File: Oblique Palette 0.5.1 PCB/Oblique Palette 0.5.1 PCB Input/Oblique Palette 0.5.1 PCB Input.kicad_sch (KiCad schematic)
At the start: 24 parts

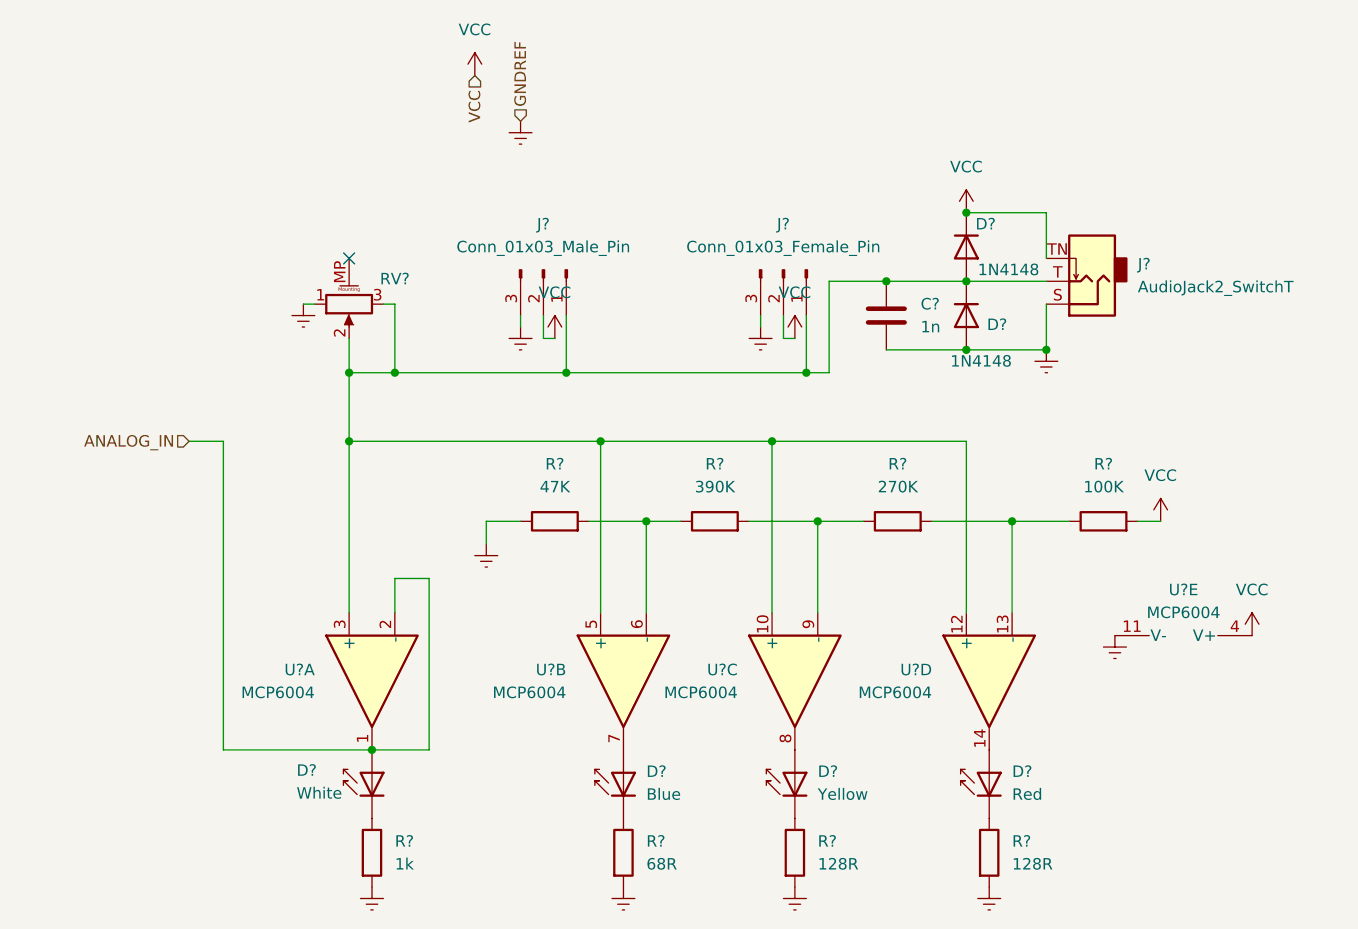
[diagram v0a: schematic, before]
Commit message: PCB corrections for 0.5.3
• Main output LED is now between op amp and feedback loop, so it will brighten at the first whiff of voltage.
• Errant wire between VBus and input potentiometer will allow us to have signals other than 5V
• Servos are now powered by V_SERVO as well as VBus.

TO DO: Differentiate A0 and A1 DACs
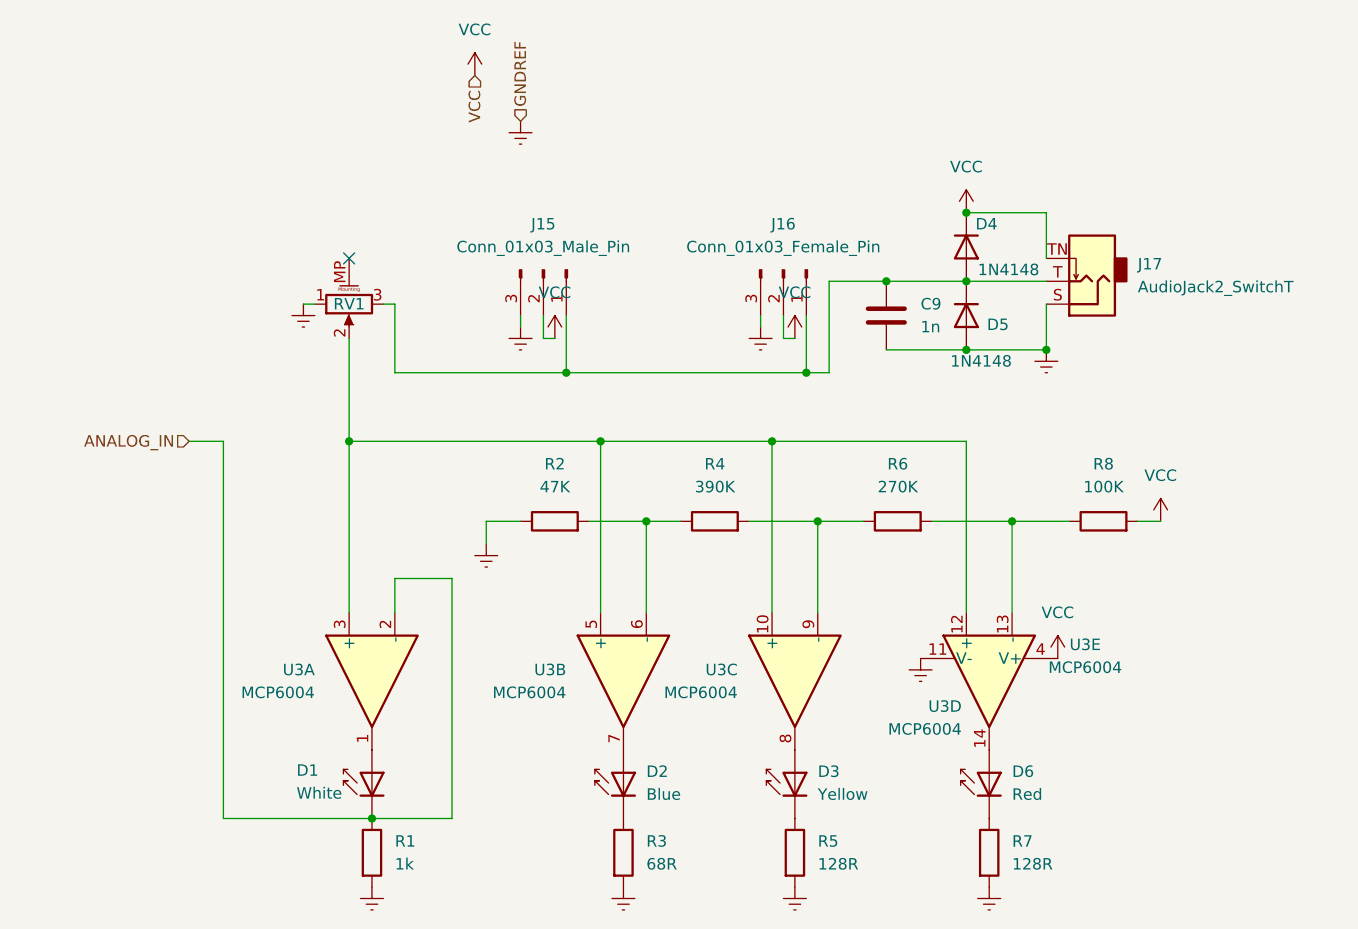
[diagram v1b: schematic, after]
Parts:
- gave numbers to parts that had none: 20
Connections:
- net ANALOG_IN: now also D1.1 (K), R1.1; no longer D1.2 (A), U3.1
- net at C9.1, D4.2 (A), D5.1 (K)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: no longer RV1.2, U3.10 (+), U3.12 (+), U3.3 (+), U3.5 (+)
- new net: D1.2 (A), U3.1
- new net: RV1.2, U3.10 (+), U3.12 (+), U3.3 (+), U3.5 (+)
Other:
- moved on the sheet: U3E

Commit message: Corrected op amp circuits on INPUT
Reduced from 4 LED indicators to 3, plus output.

WHITE now glows increasing brightness from >0V up to 5V
YELLOW turns on at 2.7V (a logical HIGH)
RED turns on at 3.6V (the danger level for 3V circuits)

The remaining op amp is now purely an output, now with a 1k resistor to reduce whoopsies while in use.
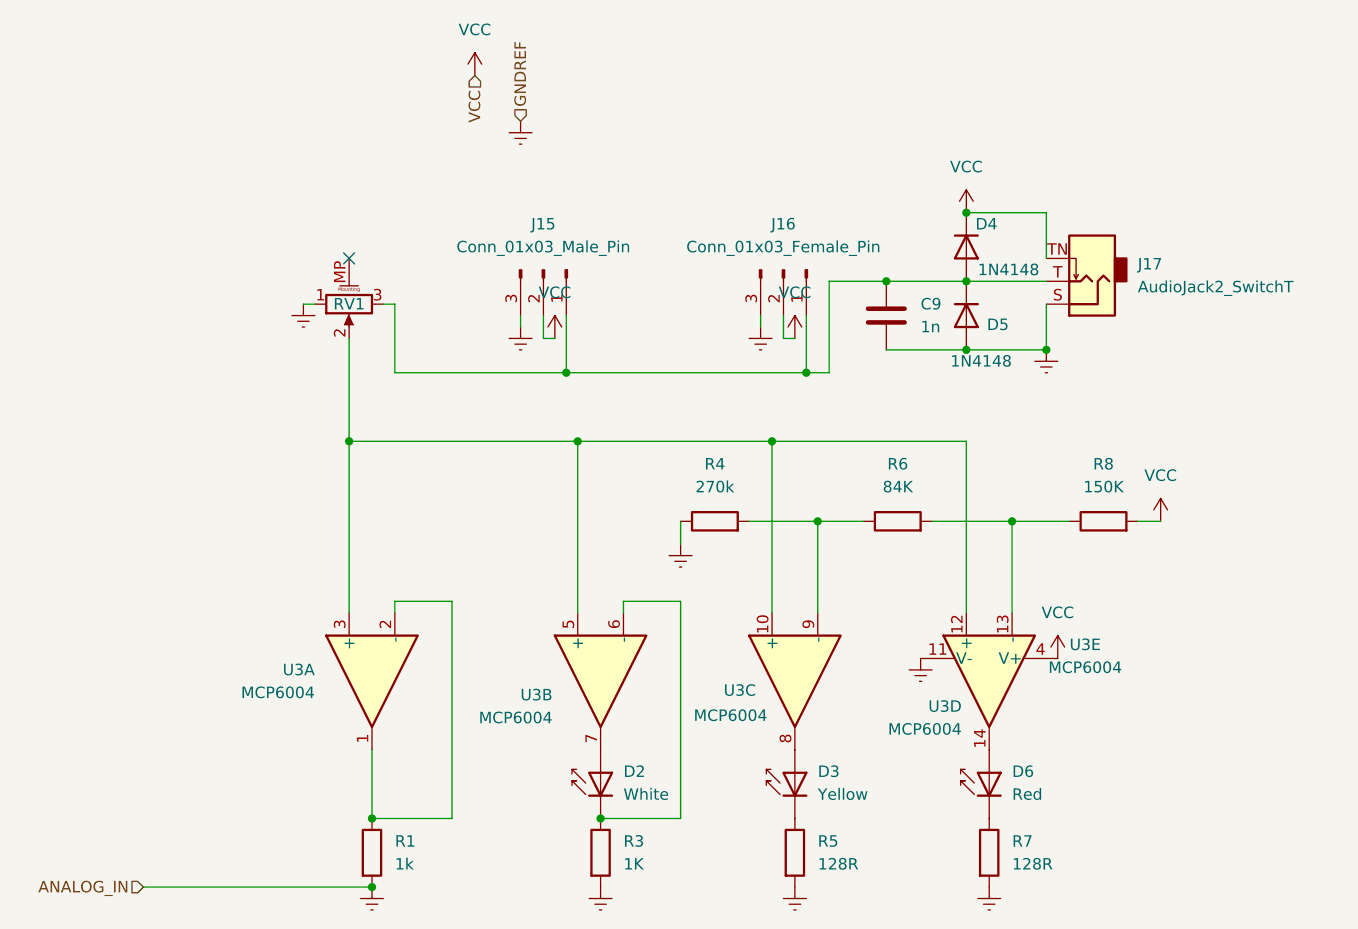
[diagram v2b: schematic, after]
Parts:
- removed D1: White, LED_THT:LED_SideEmitter_Rectangular_W4.5mm_H1.6mm, symbol LED:IRL81A
- removed R2: 47K, Resistor_SMD:R_0805_2012Metric, symbol Device:R
- D2: value Blue -> White
- R3: value 68R -> 1K
- R4: value 390K -> 270k
- R6: value 270K -> 84K
- R8: value 100K -> 150K
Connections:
- net ANALOG_IN is gone; now on an unnamed net: R1.1, U3.2 (-)
- net GNDREF: now also R4.1
- net at U3.6 (-): now also D2.1 (K), R3.1; no longer R4.1
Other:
- moved on the sheet: D2, R3, U3B

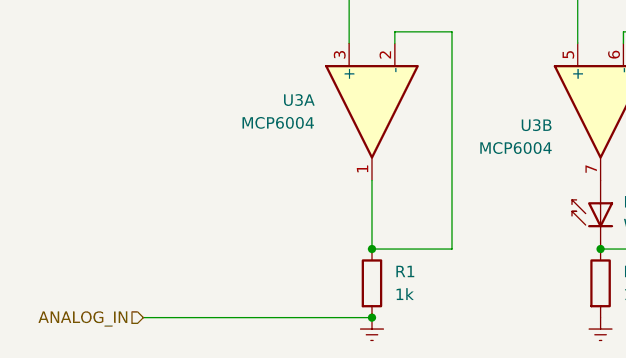
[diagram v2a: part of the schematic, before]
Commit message: Deleted redundant resistor
Realized that the input between the op amp and the µC pin didn't need a current-limiting resistor because we know exactly what's going to be there.
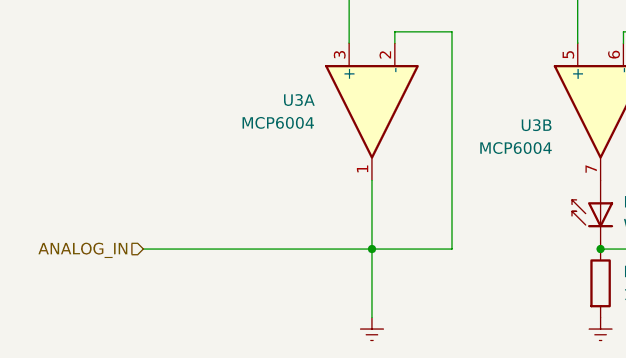
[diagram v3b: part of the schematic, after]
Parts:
- removed R1: 1k, Resistor_SMD:R_0805_2012Metric, symbol Device:R
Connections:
- net GNDREF: now also U3.1, U3.2 (-)
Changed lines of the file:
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@@
 	)
 	(junction
-		(at 105.41 128.27)
-		(diameter 0)
-		(color 0 0 0 0)
-	)
-	(junction
 		(at 149.86 78.74)
 		(diameter 0)
@@
 	(wire
 		(pts
-			(xy 80.01 128.27) (xy 105.41 128.27)
+			(xy 80.01 120.65) (xy 105.41 120.65)
 		)
 		(stroke
@@
 	(wire
 		(pts
+			(xy 105.41 120.65) (xy 105.41 128.27)
+		)
+		(stroke
+			(width 0)
+			(type default)
+		)
+	)
+	(wire
+		(pts
 			(xy 176.53 87.63) (xy 176.53 97.79)
 		)
@@
 	(hierarchical_label "ANALOG_IN"
 		(shape input)
-		(at 80.01 128.27 180)
+		(at 80.01 120.65 180)
 		(effects
 			(font
@@
 					(unit 1)
 				)
-			)
-		)
-	)
-	(symbol
-		(lib_id "Device:R")
-		(at 105.41 124.46 0)
-		(unit 1)
-		(exclude_from_sim no)
-		(in_bom yes)
-		(on_board yes)
-		(dnp no)
-		(fields_autoplaced yes)
-		(property "Reference" "R1"
-			(at 107.95 123.1899 0)
-			(effects
-				(font
-					(size 1.27 1.27)
-				)
-				(justify left)
-			)
-		)
-		(property "Value" "1k"
-			(at 107.95 125.7299 0)
-			(effects
-				(font
-					(size 1.27 1.27)
-				)
-				(justify left)
-			)
-		)
-		(property "Footprint" "Resistor_SMD:R_0805_2012Metric"
-			(at 103.632 124.46 90)
-			(effects
-				(font
-					(size 1.27 1.27)
-				)
-				(hide yes)
-			)
-		)
-		(property "Datasheet" "~"
-			(at 105.41 124.46 0)
-			(effects
-				(font
-					(size 1.27 1.27)
-				)
-				(hide yes)
-			)
-		)
-		(property "Description" "Resistor"
-			(at 105.41 124.46 0)
-			(effects
-				(font
-					(size 1.27 1.27)
-				)
-				(hide yes)
-			)
-		)
-		(pin "2"
-		)
-		(pin "1"
-		)
-		(instances
-			(project "Oblique Palette 0.4 Input Stage"
-				(path "/150b6f87-53bb-44d6-889a-48fbcb7c0f5a"
-					(reference "R?")
-					(unit 1)
-				)
-			)
-			(project "Oblique Palette 0.5.1 PCB Main"
-				(path "/28718c51-05fa-44bf-9e59-30883fb9ecef/10bc258e-81e1-44f3-990d-192650ef1d17"
-					(reference "R25")
-					(unit 1)
-				)
-				(path "/28718c51-05fa-44bf-9e59-30883fb9ecef/57e02da9-4257-4ca7-873b-16131b7a2160"
-					(reference "R9")
-					(unit 1)
-				)
-				(path "/28718c51-05fa-44bf-9e59-30883fb9ecef/7745d2af-7356-4abb-bb12-892bad795ddc"
-					(reference "R57")
-					(unit 1)
-				)
-				(path "/28718c51-05fa-44bf-9e59-30883fb9ecef/987e670c-6148-4b51-9cfd-5f14311b6128"
-					(reference "R49")
-					(unit 1)
-				)
-				(path "/28718c51-05fa-44bf-9e59-30883fb9ecef/b5a2c36a-8809-438c-979e-3df70d5c3577"
-					(reference "R41")
-					(unit 1)
-				)
-				(path "/28718c51-05fa-44bf-9e59-30883fb9ecef/b606fcb4-531c-4aac-8b9c-456946edc41a"
-					(reference "R17")
-					(unit 1)
-				)
-				(path "/28718c51-05fa-44bf-9e59-30883fb9ecef/f139377a-d7a4-4f83-81e4-8f98ca8ad38f"
-					(reference "R1")
-					(unit 1)
-				)
-				(path "/28718c51-05fa-44bf-9e59-30883fb9ecef/f541c48a-fb18-4fa4-aa45-9d69b2f53442"
-					(reference "R33")
-					(unit 1)
-				)

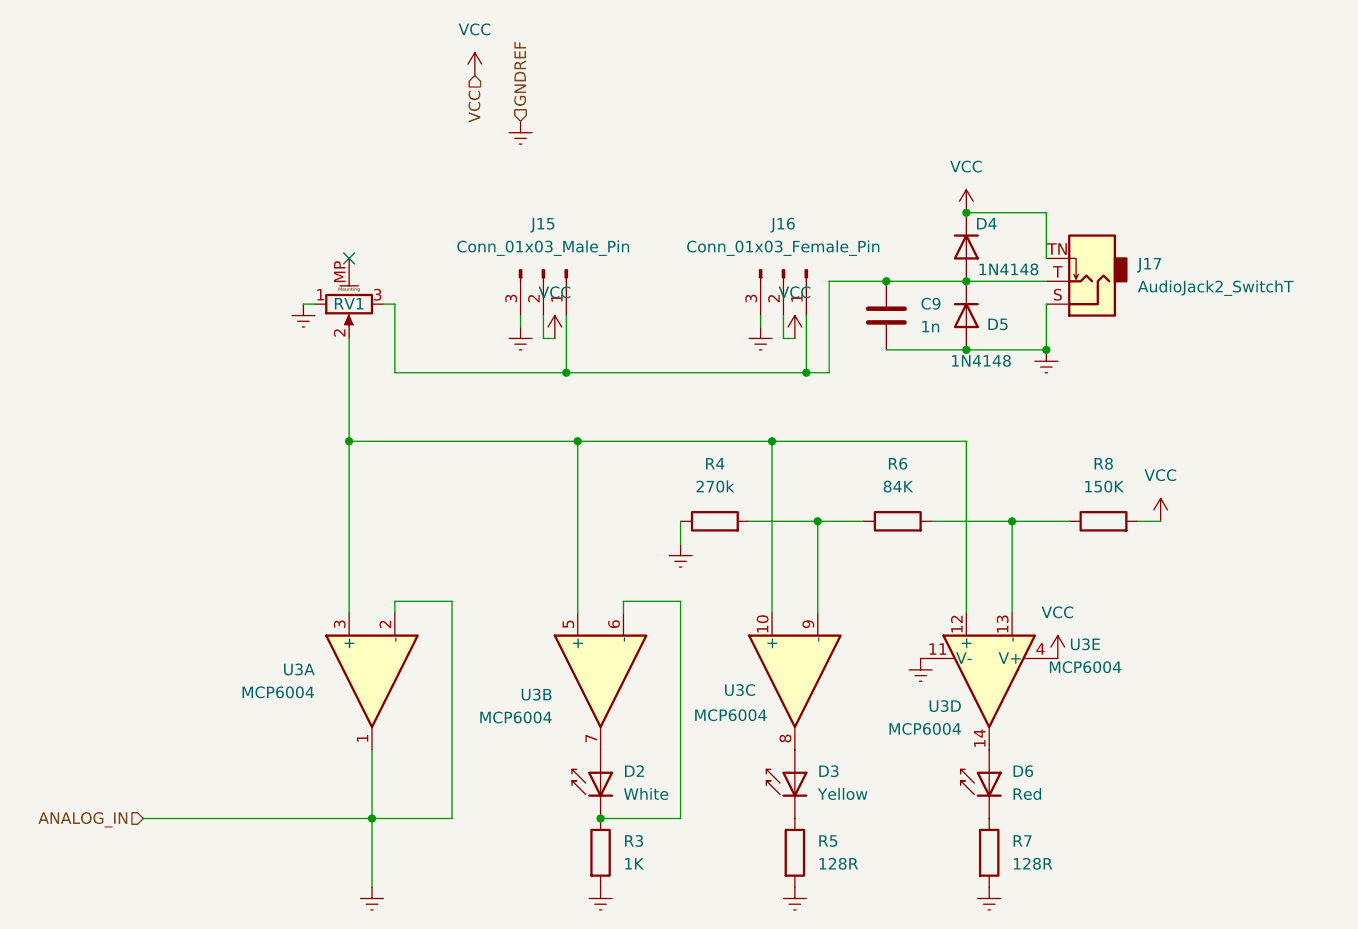
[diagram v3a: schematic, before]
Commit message: More input and output channel corrections
Reduced the white LED inputs to have a range of 0V:3.3V to get a greater range of brightness across the range of values

Powered the input op amps from 3v3 so we can't blow up. Changed the comparison voltage for the LEDs to 0V:3.3V instead of up to 5 so brightnesses are consistent between input and output channels.
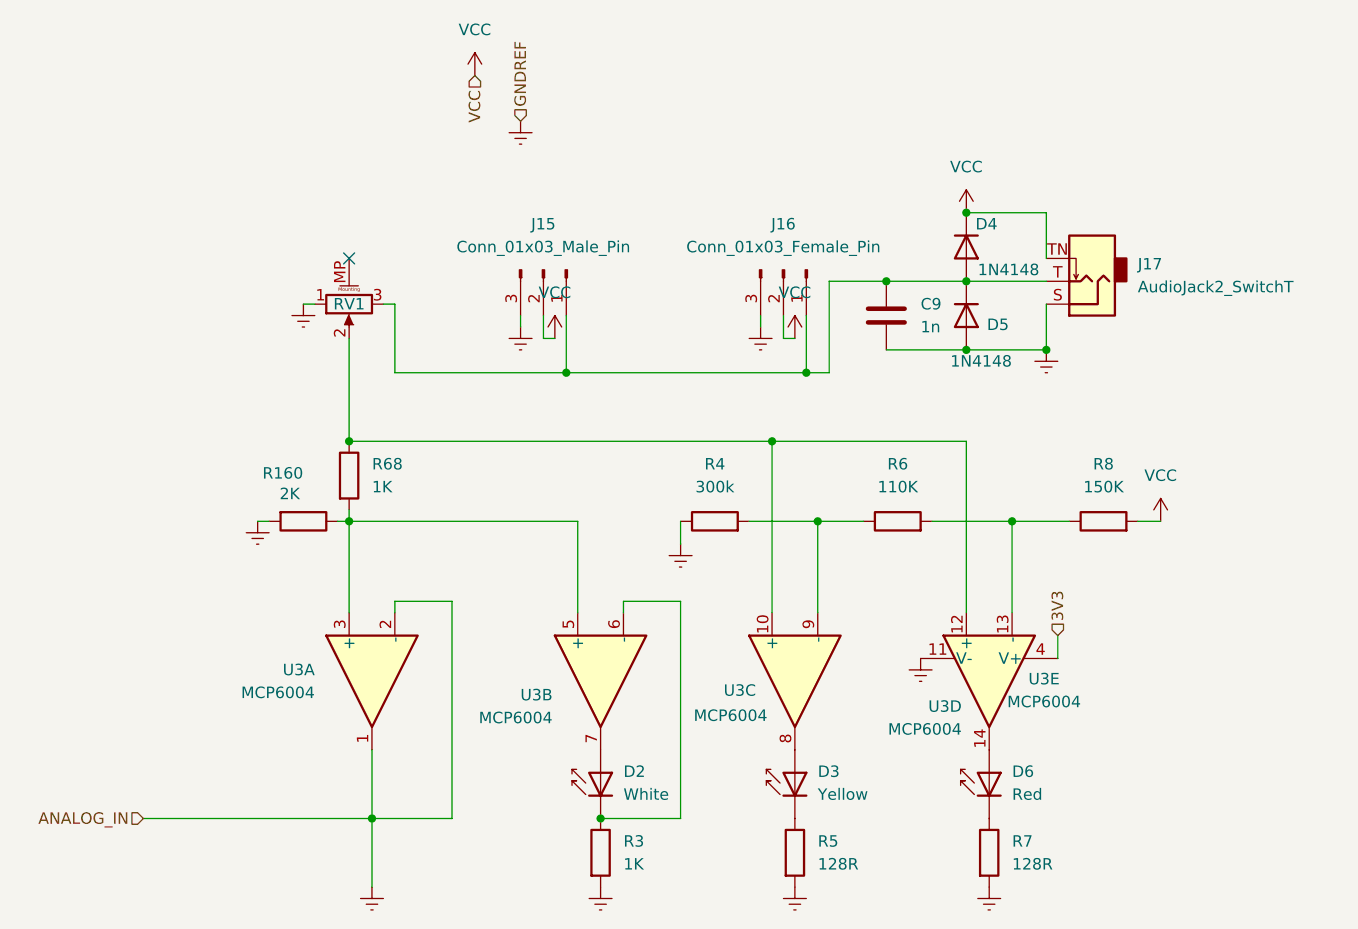
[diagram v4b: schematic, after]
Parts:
- added R160: 2K, Resistor_SMD:R_0805_2012Metric, symbol Device:R
- added R68: 1K, Resistor_SMD:R_0805_2012Metric, symbol Device:R
- R4: value 270k -> 300k
- R6: value 84K -> 110K
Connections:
- net GNDREF: now also R160.2
- net VCC: no longer U3.4 (V+)
- net at RV1.2, U3.10 (+), U3.12 (+): now also R68.1; no longer U3.3 (+), U3.5 (+)
- new net: R160.1, R68.2, U3.3 (+), U3.5 (+)
- new net 3V3: U3.4 (V+)

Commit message: Front panel channel labels
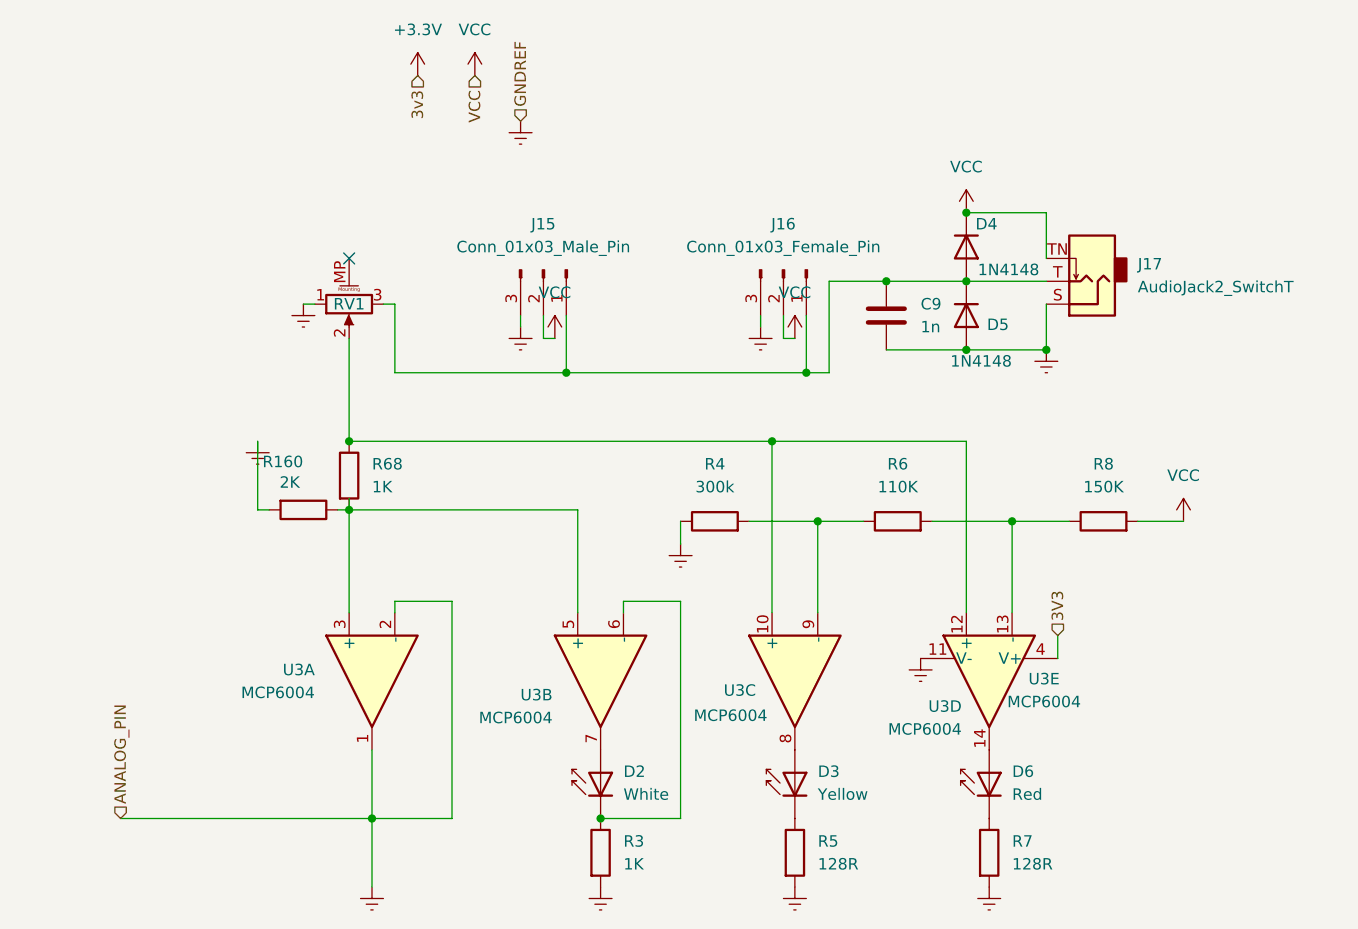
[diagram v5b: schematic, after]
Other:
- moved on the sheet: R160
